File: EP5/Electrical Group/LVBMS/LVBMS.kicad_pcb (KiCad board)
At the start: 2 copper layers, 43.9 x 27.4 mm, 14 parts, among them J1 BAT, J2 OUT, Q1 IRF4905, U1 LM317_TO-220, U3 LM741

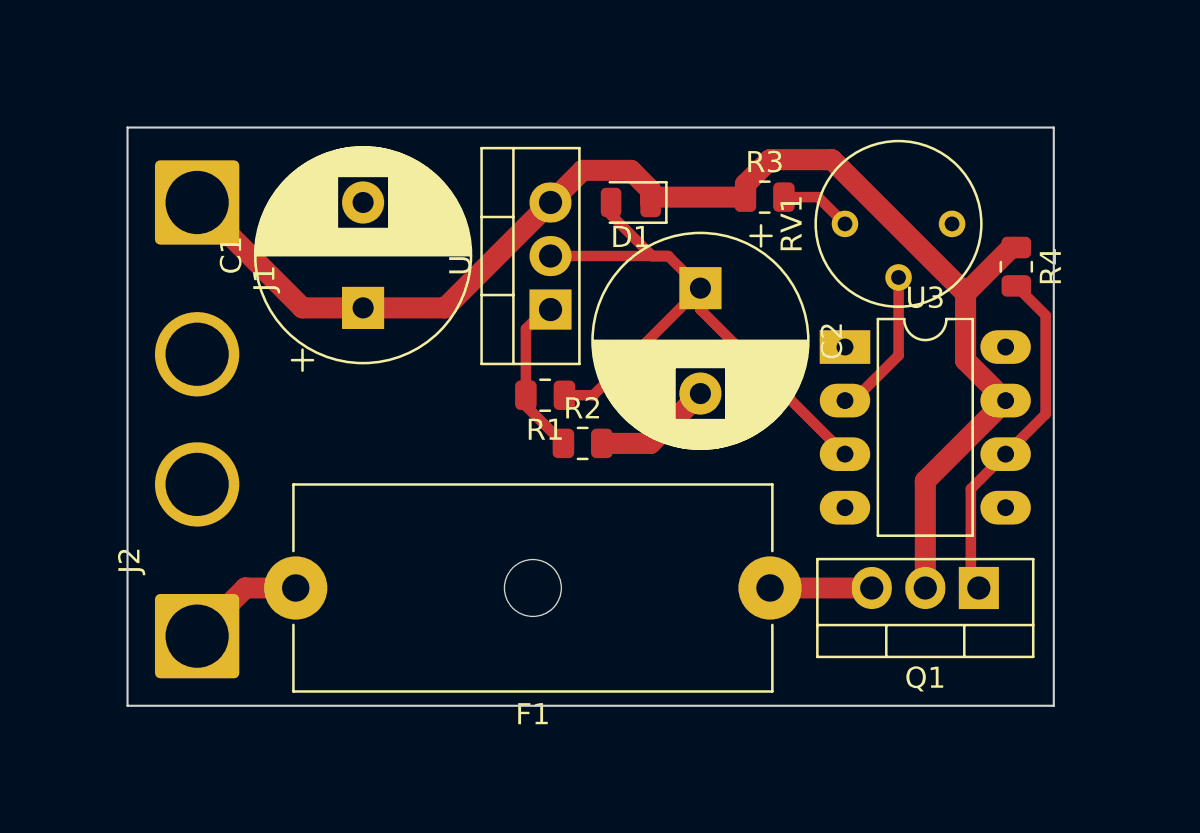
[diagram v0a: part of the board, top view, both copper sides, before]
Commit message: big update
new power board
update: LVBMS, dashbaord box connector boards *2
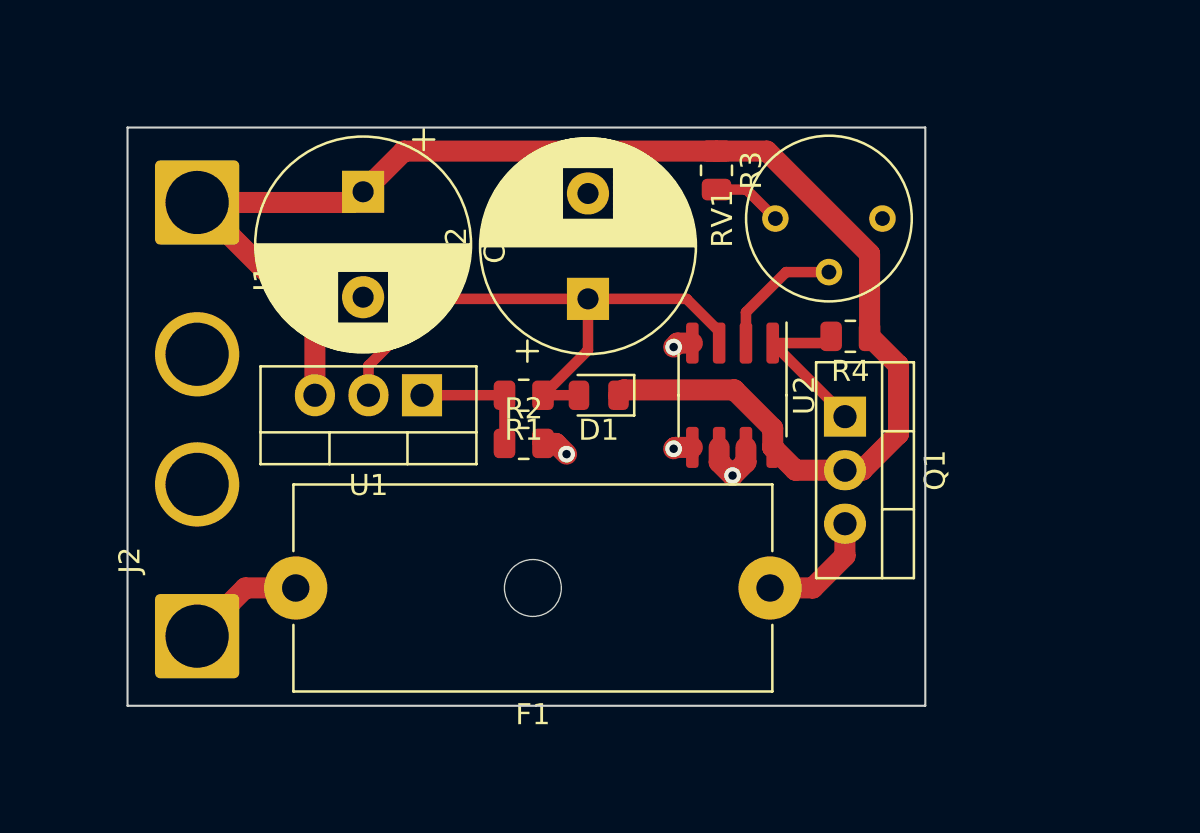
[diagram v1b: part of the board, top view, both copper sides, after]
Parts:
- removed U3: LM741, Package_DIP:DIP-8_W7.62mm_LongPads
- added U2: LM2903, Package_SO:SOIC-8_3.9x4.9mm_P1.27mm, F.Cu at (108.7, 72.9)
- moved Q1 10.3 mm to (114.0, 73.9), turned to -90 degrees
- moved D1 9.27 mm to (102.4, 72.9)
- moved R4 8.54 mm to (114.3, 70.1), turned to 180 degrees
- moved U1 7.33 mm to (94.0, 72.9), turned to 180 degrees
- moved C1 5.51 mm to (91.2, 63.2), turned to -90 degrees
- moved C2 5.36 mm to (101.9, 68.3), turned to 90 degrees
- moved RV1 3.31 mm to (115.8, 64.5)
- moved R2 2.79 mm to (98.8, 75.2)
- moved R3 2.62 mm to (108.0, 62.2), turned to -90 degrees
- moved R1 1.02 mm to (98.8, 72.9)
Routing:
- net Net-(Q1-G): track 16.5 -> 7.81 mm
- net +24V: track 65.7 -> 71.7 mm
- net Net-(D1-A): track 31.1 -> 27.7 mm
- net Net-(U1-ADJ): track 7.72 -> 6.20 mm
- net Net-(U2A--): track 7.13 -> 6.19 mm
- net Net-(Q1-S): track 4.83 -> 5.71 mm
- net GNDPWR: track 5.66 -> 6.41 mm, vias 0 -> 4
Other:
- board size 43.9 x 27.4 mm -> 37.8 x 27.4 mm

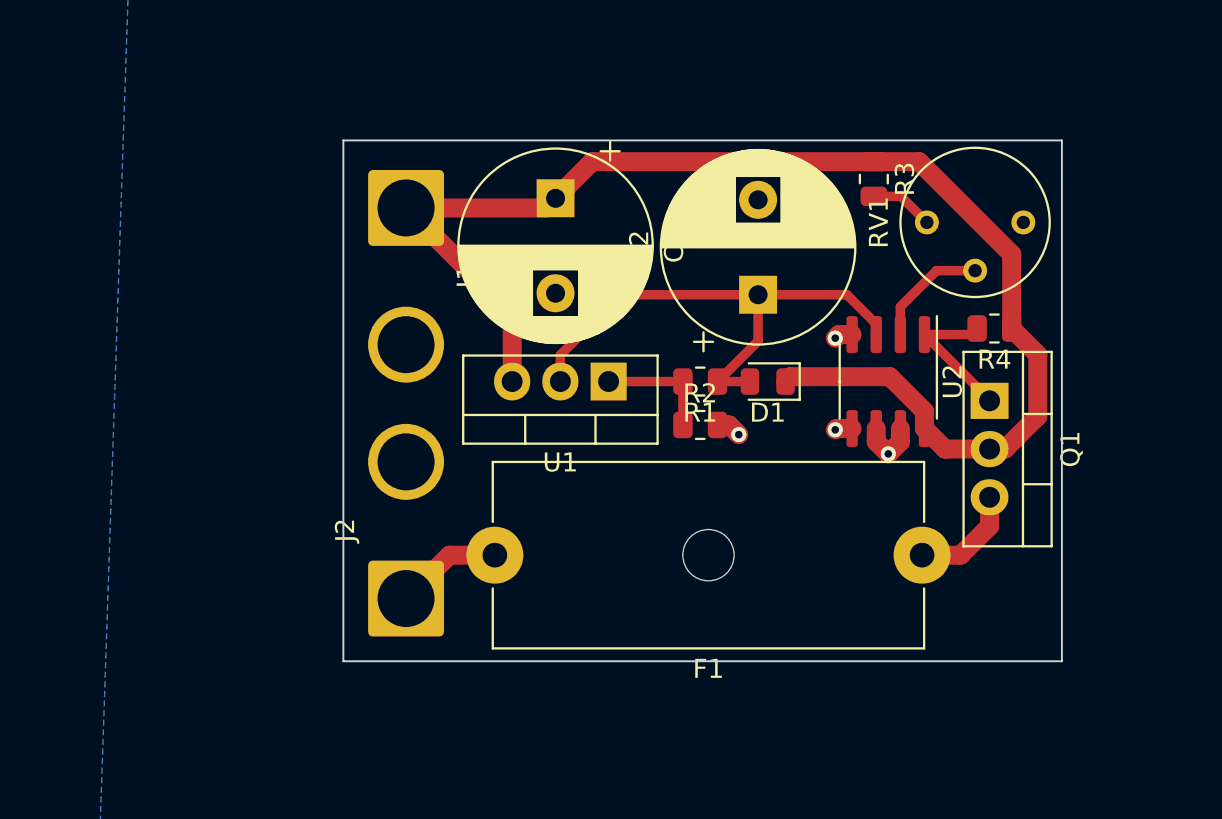
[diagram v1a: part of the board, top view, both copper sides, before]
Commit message: update boards in rear box after Tsou's review
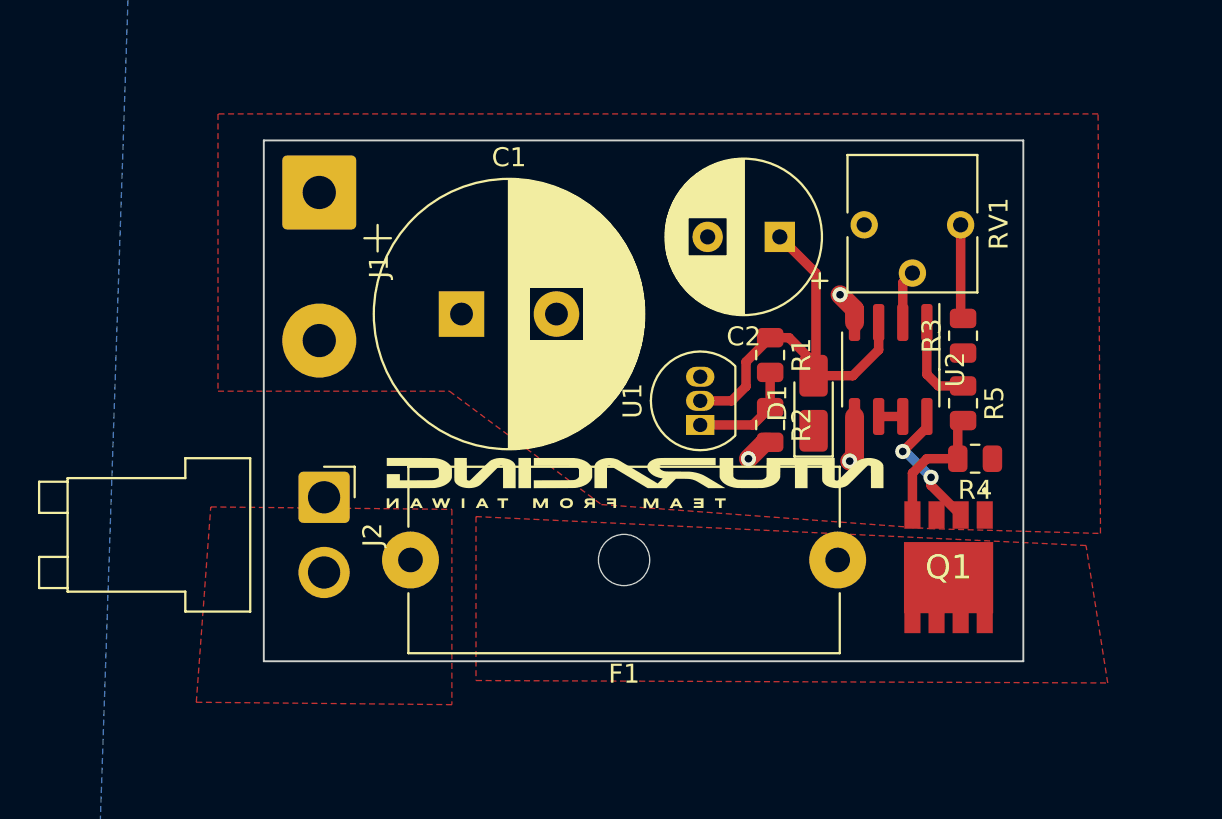
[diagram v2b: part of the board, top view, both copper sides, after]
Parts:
- added R5: 10k, Resistor_SMD:R_0805_2012Metric, F.Cu at (112.6, 74.0)
- C1: footprint Capacitor_THT:CP_Radial_D10.0mm_P5.00mm -> Capacitor_THT:CP_Radial_D14.0mm_P5.00mm
- C2: footprint Capacitor_THT:CP_Radial_D10.0mm_P5.00mm -> Capacitor_THT:CP_Radial_D8.0mm_P3.80mm
- D1: footprint Diode_SMD:D_0805_2012Metric -> Diode_SMD:D_MicroMELF_Handsoldering
- J1: footprint Connector_Wire:SolderWire-2.5sqmm_1x02_P7.2mm_D2.4mm_OD3.6mm -> Connector_Wire:SolderWire-1sqmm_1x02_P7.8mm_D1.4mm_OD3.9mm
- J2: footprint Connector_Wire:SolderWire-2.5sqmm_1x02_P7.2mm_D2.4mm_OD3.6mm -> Connector_JST:JST_VH_B2PS-VH_1x02_P3.96mm_Horizontal
- Q1: value IRF4905 -> TPCA8120,L1Q; footprint Package_TO_SOT_THT:TO-220-3_Vertical -> SamacSys_Parts:TPH4R003NLL1Q
- RV1: footprint Potentiometer_THT:Potentiometer_Bourns_3339P_Vertical -> Potentiometer_THT:Potentiometer_Vishay_T73YP_Vertical
- U1: value LM317_TO-220 -> LM4041LP-ADJ; footprint Package_TO_SOT_THT:TO-220-3_Vertical -> Package_TO_SOT_THT:TO-92_Inline
- moved R3 9.50 mm to (112.6, 70.5), turned to 90 degrees
- moved Q1 9.03 mm to (111.9, 82.7), turned to 180 degrees
- moved RV1 8.38 mm to (107.4, 64.6), turned to -90 degrees
- moved C1 7.85 mm to (86.2, 69.3), turned to 0 degrees
- moved R4 6.93 mm to (113.3, 77.0)
- moved J2 6.86 mm to (79.0, 79.0), turned to -90 degrees
- moved U1 5.34 mm to (98.8, 75.2), turned to 90 degrees
- moved J1 4.64 mm to (78.7, 62.9)
- moved F1 4.45 mm to (106.0, 82.3)
- moved R1 3.94 mm to (102.5, 71.5), turned to -90 degrees
- moved R2 3.68 mm to (102.5, 75.2), turned to -90 degrees
- moved C2 3.26 mm to (103.0, 65.3), turned to 180 degrees
- moved D1 2.67 mm to (104.8, 74.0), turned to 90 degrees
- moved U2 0.65 mm to (108.8, 72.3)
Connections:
- F1 pad 1: Net-(Q1-S) -> /+24V_prefuse
- F1 pad 2: Net-(J2-Pin_1) -> /+24V_outbox
- J2 pad 1: Net-(J2-Pin_1) -> GNDPWR
- J2 pad 2: GNDPWR -> /+24V_outbox
- Q1 pad 1: Net-(Q1-G) -> +24V
- Q1 pad 3: Net-(Q1-S) -> +24V
- U2 pad 1: Net-(Q1-G) -> Net-(R5-Pad1)
- U2 pad 6: GNDPWR -> Net-(U2B--)
- U2 pad 7: GNDPWR -> Net-(U2B--)
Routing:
- net +24V: track 71.7 -> 7.05 mm, vias 0 -> 2
- net Net-(Q1-S): track 5.71 -> 0.00 mm
- net Net-(J2-Pin_1): track 5.62 -> 0.00 mm
- net Net-(R5-Pad1): track 0.00 -> 4.89 mm
- net Net-(D1-A): track 27.7 -> 22.9 mm
- net Net-(U2A--): track 6.19 -> 2.82 mm
- net Net-(R3-Pad2): track 3.36 -> 4.98 mm
- net Net-(U2B--): track 0.00 -> 1.27 mm
- net Net-(Q1-G): track 7.81 -> 7.03 mm
- net GNDPWR: track 6.41 -> 5.74 mm, vias 4 -> 3
- added copper zone on F.Cu, net +24V
- added copper zone on F.Cu, net /+24V_outbox
- added copper zone on F.Cu, net /+24V_prefuse
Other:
- board size 37.8 x 27.4 mm -> 40 x 27.4 mm

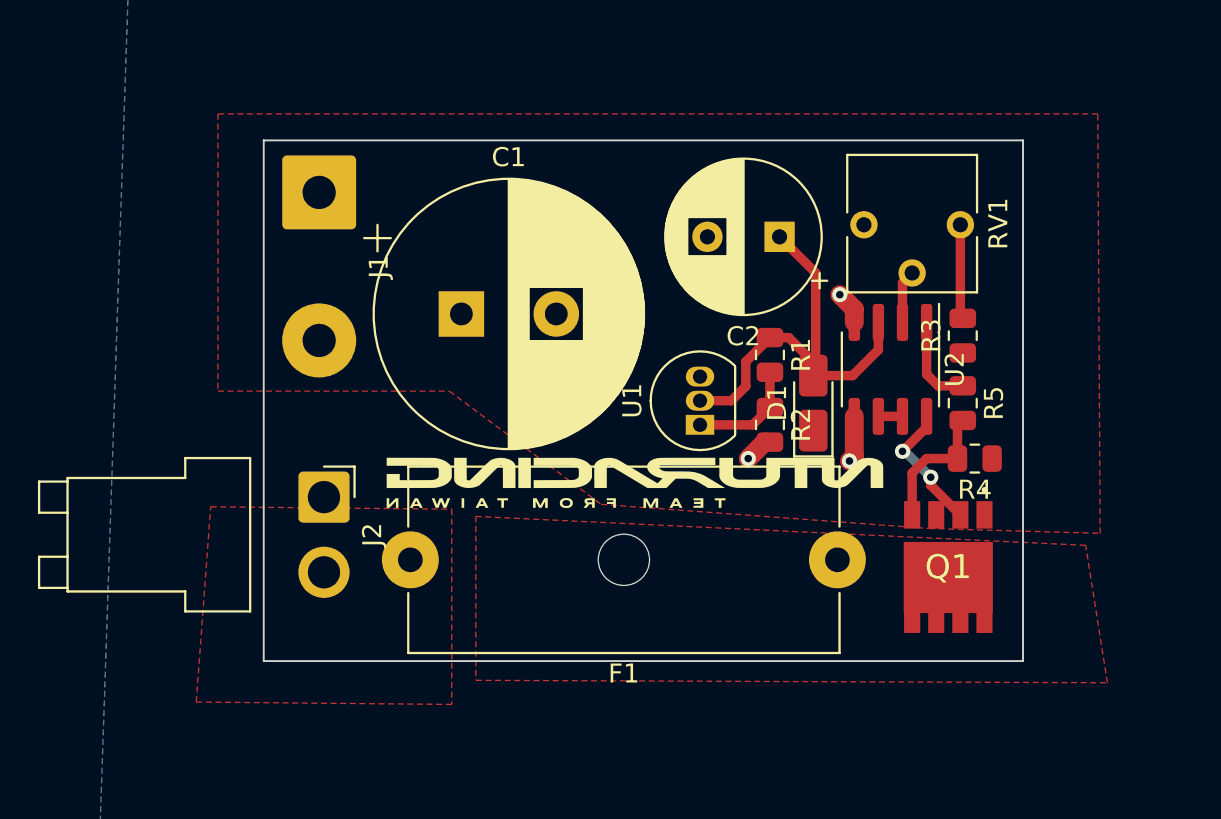
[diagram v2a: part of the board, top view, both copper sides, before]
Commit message: update all boards after Tsou's second review
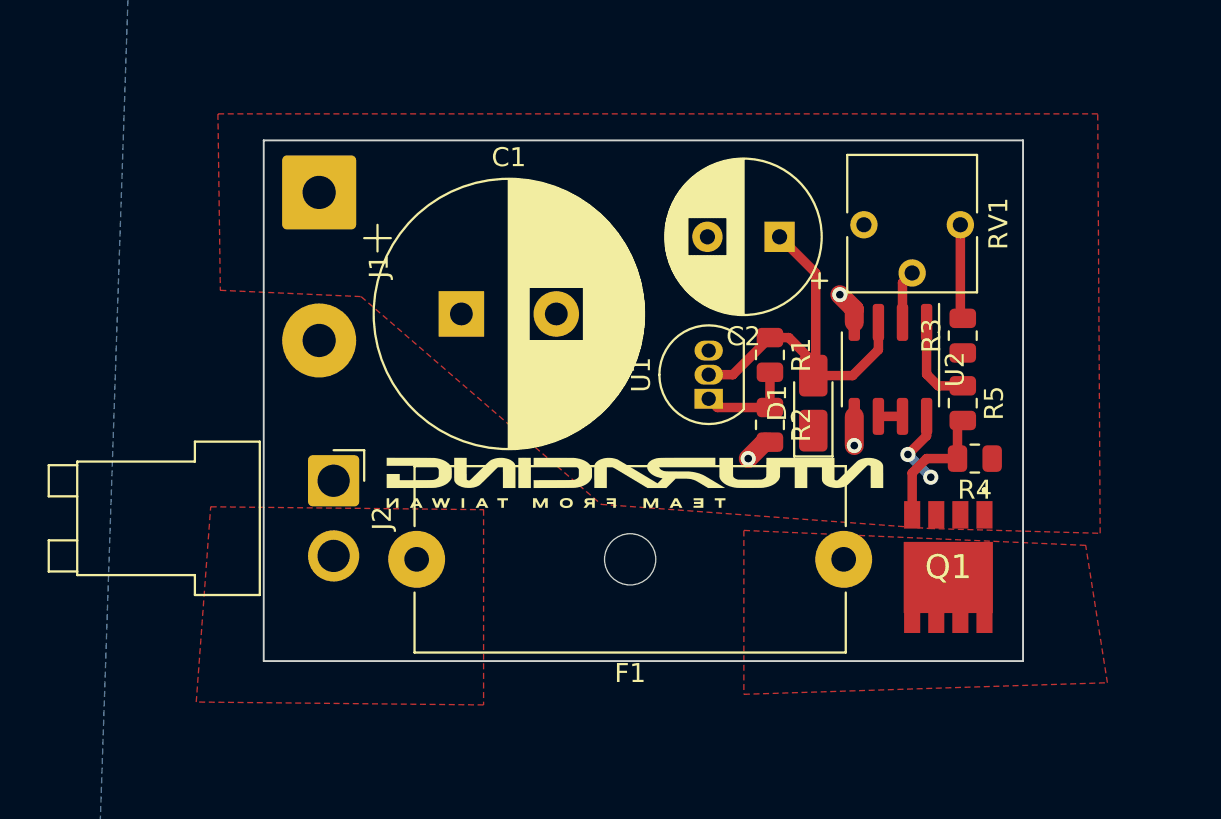
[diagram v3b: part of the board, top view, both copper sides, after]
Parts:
- moved U1 1.45 mm to (99.3, 73.8)
- moved J2 1.00 mm to (79.5, 78.1)
- moved F1 0.33 mm to (106.4, 82.3)
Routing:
- net +24V: track 7.05 -> 4.12 mm
- net Net-(D1-A): track 22.9 -> 21.2 mm
- net GNDPWR: track 5.74 -> 4.82 mm
- net Net-(U1-FB): track 5.92 -> 5.27 mm
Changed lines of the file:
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@@
   )
   (footprint "Package_TO_SOT_THT:TO-92_Inline" (layer "F.Cu")
-    (at 98.806 75.184 90)
+    (at 99.2632 73.8124 90)
     (descr "TO-92 leads in-line, narrow, oval pads, drill 0.75mm (see NXP sot054_po.pdf)")
     (tags "to-92 sc-43 sc-43a sot54 PA33 transistor")
@@
   )
   (footprint "Fuse:Fuseholder_Cylinder-5x20mm_Schurter_0031_8201_Horizontal_Open" (layer "F.Cu")
-    (at 106.045 82.296 180)
+    (at 106.3752 82.2706 180)
     (descr "Fuseholder horizontal open, 5x20mm, 500V, 16A, Schurter 0031.8201, https://us.schurter.com/bundles/snceschurter/epim/_ProdPool_/newDS/en/typ_OGN.pdf")
     (tags "Fuseholder horizontal open 5x20 Schurter 0031.8201")
@@
   )
   (footprint "Connector_JST:JST_VH_B2PS-VH_1x02_P3.96mm_Horizontal" (layer "F.Cu")
-    (at 78.994 78.994 -90)
+    (at 79.502 78.1304 -90)
     (descr "JST VH series connector, B2PS-VH (http://www.jst-mfg.com/product/pdf/eng/eVH.pdf), generated with kicad-footprint-generator")
     (tags "connector JST VH top entry")
@@
   (gr_rect (start 75.819 60.198) (end 115.824 87.63)
     (stroke (width 0.1) (type default)) (fill none) (layer "Edge.Cuts"))
-  (segment (start 110.963688 78.368688) (end 112.522 79.927) (width 0.5) (layer "F.Cu") (net 1))
-  (segment (start 110.963688 77.943688) (end 110.963688 78.368688) (width 0.5) (layer "F.Cu") (net 1))
-  (segment (start 110.744 75.311) (end 110.744 74.738) (width 0.5) (layer "F.Cu") (net 1))
-  (segment (start 109.474 76.581) (end 110.744 75.311) (width 0.5) (layer "F.Cu") (net 1))
-  (via (at 109.474 76.581) (size 0.8) (drill 0.4) (layers "F.Cu" "B.Cu") (net 1))
+  (segment (start 109.758761 76.745863) (end 110.744 75.760624) (width 0.5) (layer "F.Cu") (net 1))
+  (segment (start 110.744 75.760624) (end 110.744 74.738) (width 0.5) (layer "F.Cu") (net 1))
+  (via (at 109.758761 76.745863) (size 0.8) (drill 0.4) (layers "F.Cu" "B.Cu") (net 1))
   (via (at 110.963688 77.943688) (size 0.8) (drill 0.4) (layers "F.Cu" "B.Cu") (net 1))
-  (segment (start 109.601 76.581) (end 109.474 76.581) (width 0.5) (layer "B.Cu") (net 1))
-  (segment (start 110.963688 77.943688) (end 109.601 76.581) (width 0.5) (layer "B.Cu") (net 1))
+  (segment (start 109.758761 76.745863) (end 109.765863 76.745863) (width 0.5) (layer "B.Cu") (net 1))
+  (segment (start 109.765863 76.745863) (end 110.963688 77.943688) (width 0.5) (layer "B.Cu") (net 1))
   (segment (start 102.2115 76.0965) (end 102.489 76.0965) (width 1) (layer "F.Cu") (net 2))
   (segment (start 106.934 69.088) (end 106.172 68.326) (width 1) (layer "F.Cu") (net 2))
   (segment (start 101.346 76.962) (end 102.2115 76.0965) (width 1) (layer "F.Cu") (net 2))
-  (segment (start 106.934 76.835) (end 106.68 77.089) (width 1) (layer "F.Cu") (net 2))
+  (segment (start 106.934 76.2762) (end 106.934 74.738) (width 1) (layer "F.Cu") (net 2))
   (segment (start 106.934 69.788) (end 106.934 69.088) (width 1) (layer "F.Cu") (net 2))
-  (segment (start 106.934 74.738) (end 106.934 76.835) (width 1) (layer "F.Cu") (net 2))
-  (via (at 106.68 77.089) (size 0.8) (drill 0.4) (layers "F.Cu" "B.Cu") (net 2))
+  (via (at 106.934 76.2762) (size 0.8) (drill 0.4) (layers "F.Cu" "B.Cu") (net 2))
   (via (at 106.172 68.326) (size 0.8) (drill 0.4) (layers "F.Cu" "B.Cu") (net 2))
   (via (at 101.346 76.962) (size 0.8) (drill 0.4) (layers "F.Cu" "B.Cu") (net 2))
   (segment (start 108.204 69.788) (end 108.204 71.230528) (width 0.5) (layer "F.Cu") (net 3))
-  (segment (start 100.457 73.914) (end 101.219 73.152) (width 0.5) (layer "F.Cu") (net 3))
-  (segment (start 98.806 73.914) (end 100.457 73.914) (width 0.5) (layer "F.Cu") (net 3))
   (segment (start 104.775 72.591) (end 104.775 71.882) (width 0.5) (layer "F.Cu") (net 3))
+  (segment (start 99.2632 72.5424) (end 100.5351 72.5424) (width 0.5) (layer "F.Cu") (net 3))
   (segment (start 104.775 71.882) (end 103.4815 70.5885) (width 0.5) (layer "F.Cu") (net 3))
+  (segment (start 100.5351 72.5424) (end 102.489 70.5885) (width 0.5) (layer "F.Cu") (net 3))
   (segment (start 103.4815 70.5885) (end 102.489 70.5885) (width 0.5) (layer "F.Cu") (net 3))
-  (segment (start 101.219 71.8585) (end 102.489 70.5885) (width 0.5) (layer "F.Cu") (net 3))
   (segment (start 104.902 72.464) (end 104.775 72.591) (width 0.5) (layer "F.Cu") (net 3))
-  (segment (start 101.219 73.152) (end 101.219 71.8585) (width 0.5) (layer "F.Cu") (net 3))
   (segment (start 108.204 71.230528) (end 106.843528 72.591) (width 0.5) (layer "F.Cu") (net 3))
   (segment (start 104.902 67.183) (end 104.902 72.464) (width 0.5) (layer "F.Cu") (net 3))
@@
   (segment (start 111.3555 73.1285) (end 110.744 72.517) (width 0.5) (layer "F.Cu") (net 9))
   (segment (start 112.649 73.1285) (end 111.3555 73.1285) (width 0.5) (layer "F.Cu") (net 9))
-  (segment (start 98.806 75.184) (end 101.5765 75.184) (width 0.5) (layer "F.Cu") (net 10))
   (segment (start 102.489 72.4135) (end 102.489 74.2715) (width 0.5) (layer "F.Cu") (net 10))
-  (segment (start 101.5765 75.184) (end 102.489 74.2715) (width 0.5) (layer "F.Cu") (net 10))
+  (segment (start 99.7223 74.2715) (end 102.489 74.2715) (width 0.5) (layer "F.Cu") (net 10))
+  (segment (start 99.2632 73.8124) (end 99.7223 74.2715) (width 0.5) (layer "F.Cu") (net 10))
   (segment (start 108.204 74.738) (end 109.474 74.738) (width 0.5) (layer "F.Cu") (net 11))
   (zone (net 8) (net_name "/+24V_prefuse") (layer "F.Cu") (hatch edge 0.5)
@@
       (pts
         (xy 119.126 81.534)
-        (xy 86.995 80.01)
-        (xy 86.995 88.646)
+        (xy 101.1174 80.7466)
+        (xy 101.1174 89.3826)
         (xy 120.269 88.773)
       )
@@
       (pts
         (xy 73.025 79.502)
-        (xy 85.725 79.629)
-        (xy 85.725 89.916)
+        (xy 87.4014 79.6544)
+        (xy 87.4014 89.9414)
         (xy 72.263 89.789)
       )
@@
     (polygon
       (pts
-        (xy 85.598 73.406)
+        (xy 80.9498 68.4276)
         (xy 93.599 79.375)
         (xy 110.871 80.645)
@@
         (xy 119.761 58.801)
         (xy 73.406 58.801)
-        (xy 73.406 73.406)
+        (xy 73.533 68.0974)
       )
     )
